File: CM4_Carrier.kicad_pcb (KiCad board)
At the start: 4 copper layers, 40 x 55 mm, 74 parts, among them J1 SM04B-GHS-TB(LF)(SN)-, J10 SM06B-GHS-TB(LF)(SN), J2 USB_C_Receptacle, J3 SM04B-GHS-TB(LF)(SN)-, J4 XT30, J5 Molex 470531000, J6 Conn_01x22_Female, J7 Conn_01x22_Female, J8 Conn_02x08_Odd_Even, J9 Micro_SD_Card_Det, Q1 DMP3013SFV-7, SW1 SW_SPST, U1 FSUSB42MUX, U2 USB2514B-I/M2, U3 TPD4EUSB30, U4 LMR33640DDDAR, U5 EMC2301-1-ACZL-TR, U6 74LVC1G07SE-7, U7 RT9742GGJ5, Y1 ECS-240-18-33-JGN-TR

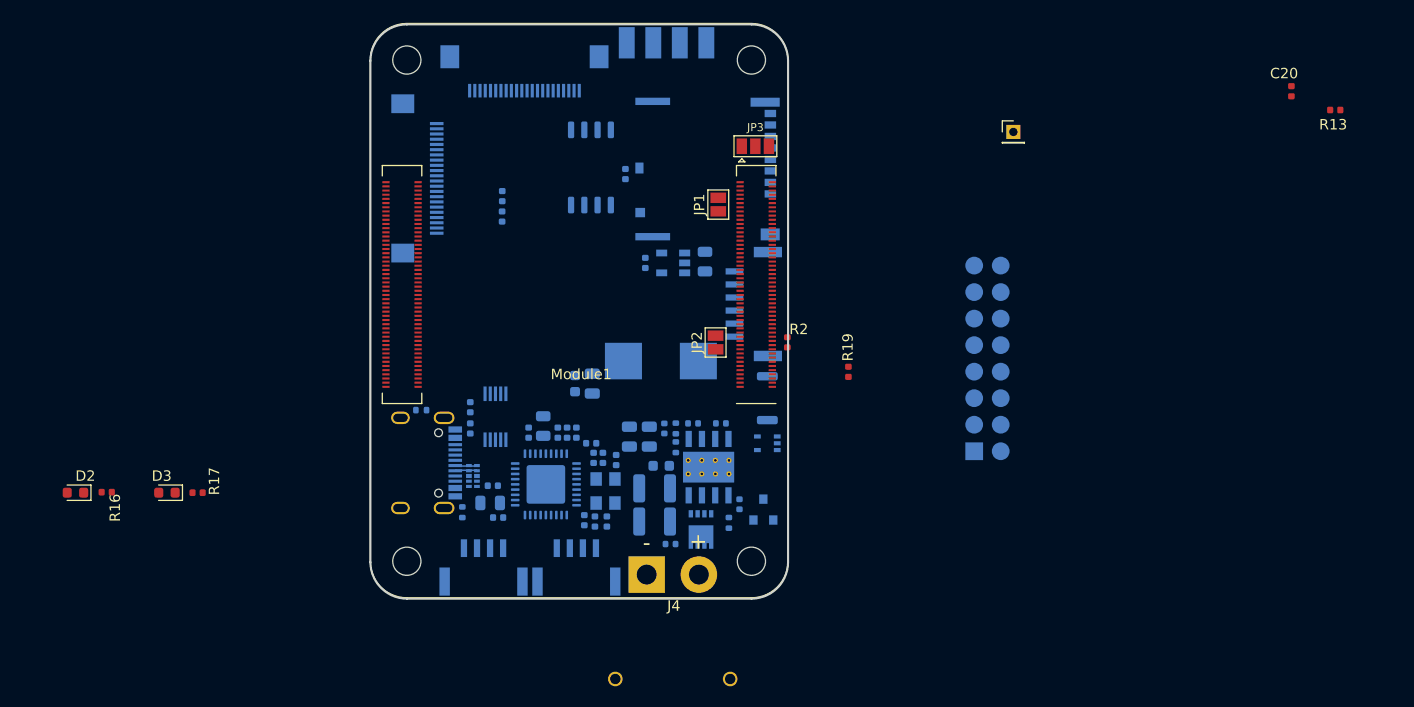
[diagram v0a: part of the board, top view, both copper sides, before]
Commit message: added components for new DC/DC regulator
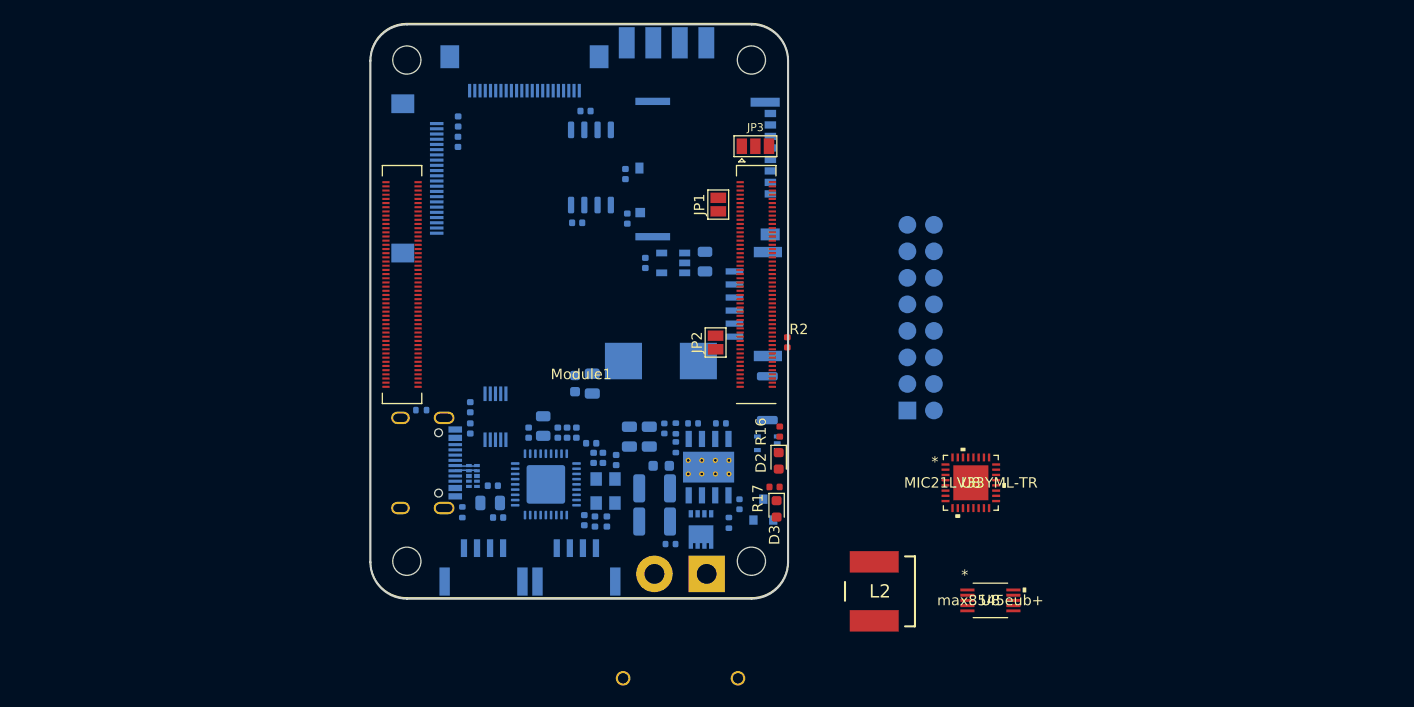
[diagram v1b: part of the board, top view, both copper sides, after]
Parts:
- removed TP1: TestPoint, Connector_PinHeader_2.00mm:PinHeader_1x01_P2.00mm_Vertical
- added L2: SRP0620-4R7K, SamacSys_Parts:SRP06204R7K, F.Cu at (162.3, 124.8)
- added U8: MIC21LV33YML-TR, Open-HD:MIC21LV33YML-TR, F.Cu at (171.0, 114.4)
- added U8: max8545eub+, Open-HD:max8545eub&plus_, F.Cu at (172.9, 125.7)
- C20, J4, R13, R19: moved to B.Cu
- moved R13 71.8 mm to (134.1, 78.8), turned to 0 degrees
- moved C20 69.6 mm to (133.3, 89.5), turned to 180 degrees
- moved D2 67.4 mm to (152.6, 112.3), turned to -90 degrees
- moved R16 64.7 mm to (152.7, 109.5), turned to 90 degrees
- moved D3 58.4 mm to (152.4, 116.9), turned to -90 degrees
- moved R17 55.3 mm to (152.2, 114.8), turned to 180 degrees
- moved R19 25.8 mm to (138.1, 89.1), turned to 90 degrees
- moved R15 8.31 mm to (121.9, 81.8)
- moved R14 8.31 mm to (121.9, 79.8)
- moved J8 7.50 mm to (164.9, 107.5)
- moved J4 5.75 mm to (145.7, 123.1), turned to 0 degrees
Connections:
- net /CAM_GPIO renamed /CM4_HighSpeed/CAM_GPIO
- net /ID_SC renamed /CM4_GPIO ( Ethernet, GPIO, SDCARD)/ID_SC
- net /ID_SD renamed /CM4_GPIO ( Ethernet, GPIO, SDCARD)/ID_SD
- net /SCL0 renamed /CM4_HighSpeed/SCL0
- net /SDA0 renamed /CM4_HighSpeed/SDA0
- net /TV_OUT renamed /CM4_HighSpeed/TV_OUT
- net /USB2_N renamed /CM4_HighSpeed/USB2_N
- net /USB2_P renamed /CM4_HighSpeed/USB2_P
- net /USBOTG renamed /CM4_HighSpeed/USBOTG_ID
- J10 pad 4: Net-(J10-Pad4) -> unconnected-(J10-Pad4)
- J10 pad 5: Net-(J10-Pad5) -> unconnected-(J10-Pad5)
- J2 pad A8: Net-(J2-PadA8) -> unconnected-(J2-PadA8)
- J2 pad B8: Net-(J2-PadB8) -> unconnected-(J2-PadB8)
- J6 pad 11: Net-(J6-Pad11) -> unconnected-(J6-Pad11)
- J6 pad 12: Net-(J6-Pad12) -> unconnected-(J6-Pad12)
- J6 pad 14: Net-(J6-Pad14) -> unconnected-(J6-Pad14)
- J6 pad 15: Net-(J6-Pad15) -> unconnected-(J6-Pad15)
- J6 pad 18: Net-(J6-Pad18) -> unconnected-(J6-Pad18)
- J7 pad 18: Net-(J7-Pad18) -> unconnected-(J7-Pad18)
- Module1 pad 104: Net-(Module1-Pad104) -> unconnected-(Module1-Pad104)
- Module1 pad 106: Net-(Module1-Pad106) -> unconnected-(Module1-Pad106)
- Module1 pad 19: Net-(Module1-Pad19) -> unconnected-(Module1-Pad19)
- Module1 pad 64: Net-(Module1-Pad64) -> unconnected-(Module1-Pad64)
- Module1 pad 68: Net-(Module1-Pad68) -> unconnected-(Module1-Pad68)
- Module1 pad 70: Net-(Module1-Pad70) -> unconnected-(Module1-Pad70)
- Module1 pad 72: Net-(Module1-Pad72) -> unconnected-(Module1-Pad72)
- Module1 pad 73: Net-(Module1-Pad73) -> unconnected-(Module1-Pad73)
- U2 pad 11: Net-(U2-Pad11) -> unconnected-(U2-Pad11)
- U2 pad 14: Net-(U2-Pad14) -> unconnected-(U2-Pad14)
- U2 pad 16: Net-(U2-Pad16) -> unconnected-(U2-Pad16)
- U2 pad 18: Net-(U2-Pad18) -> unconnected-(U2-Pad18)
- U2 pad 20: Net-(U2-Pad20) -> unconnected-(U2-Pad20)
- U2 pad 34: Net-(U2-Pad34) -> unconnected-(U2-Pad34)
- U4 pad 4: Net-(U4-Pad4) -> unconnected-(U4-Pad4)
- U5 pad 7: Net-(U5-Pad7) -> unconnected-(U5-Pad7)
- U5 pad 8: Net-(U5-Pad8) -> unconnected-(U5-Pad8)
- U7 pad 3: Net-(U7-Pad3) -> unconnected-(U7-Pad3)
